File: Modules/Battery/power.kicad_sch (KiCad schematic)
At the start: 36 parts, among them IC3 TPS630701RNMR, J2 BATTERY, J3 POWER SWITCH, J4 TEMP SENSOR, Q1 T2N7002AK,LM, U203 AP2112K-3.3, U4 BQ24075RGT

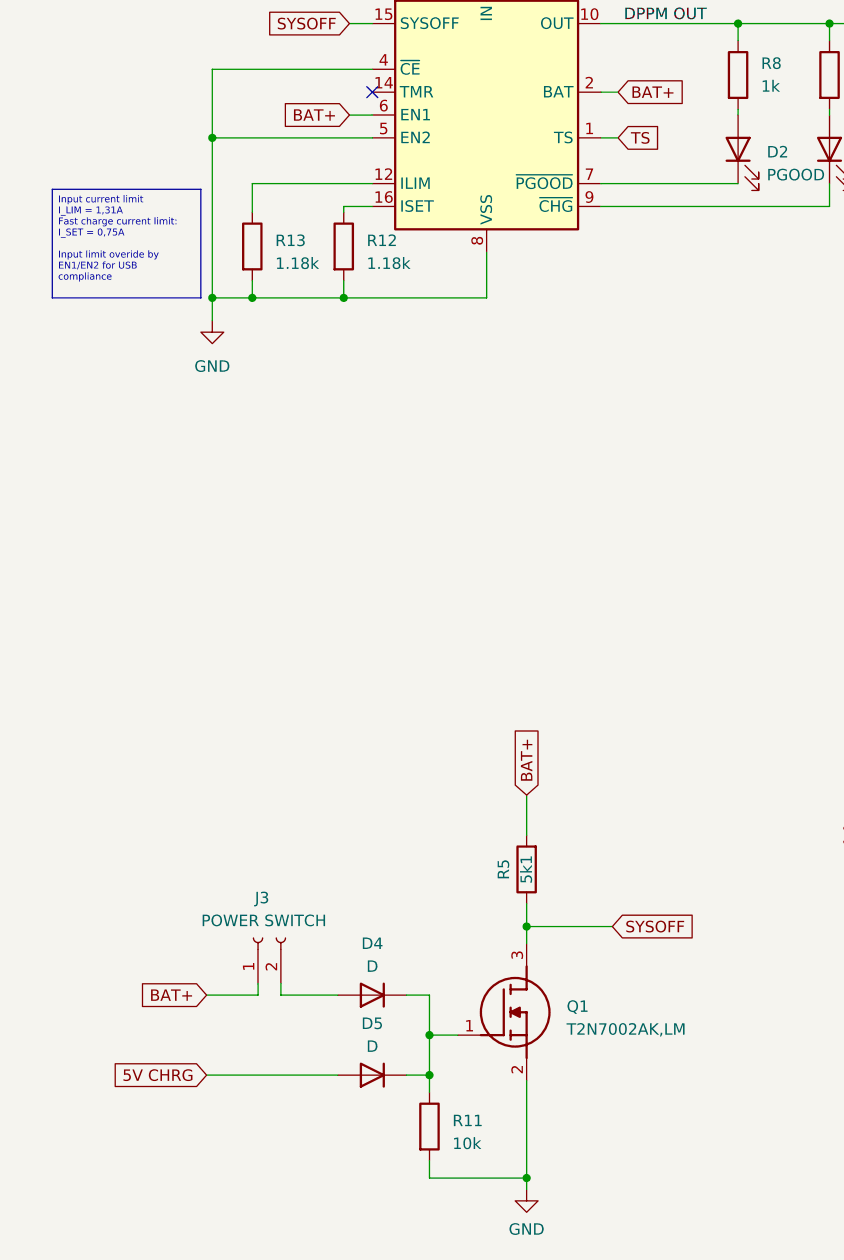
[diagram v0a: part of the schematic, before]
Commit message: update to I2C and MIDI Interface
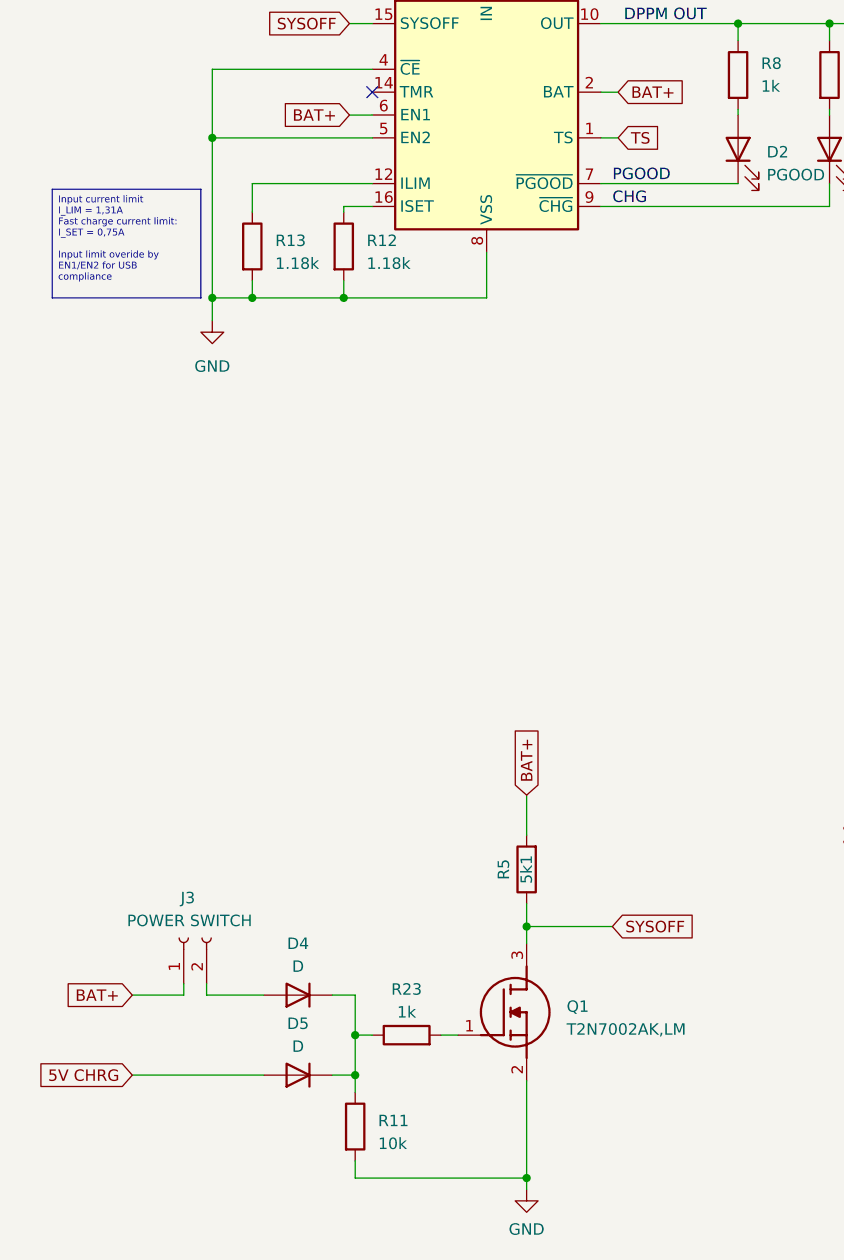
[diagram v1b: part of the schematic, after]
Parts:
- added R23: 1k, symbol Device:R
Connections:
- net CHG: now reaches D3.1 (K), U4.9 (~{CHG})
- net at D4.1 (K), D5.1 (K), R11.1: now also R23.1; no longer Q1.1 (G)
- net PGOOD: now reaches D2.1 (K), U4.7 (~{PGOOD})
- new net: Q1.1 (G), R23.2
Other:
- moved on the sheet: D4, D5, J3, R11

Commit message: first rev of Battery module
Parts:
- removed J3: POWER SWITCH, Connector_custom:PinHeader_1x02_P2.54mm_Horizontal_SMD, symbol Connector:Conn_01x02_Socket
- removed J4: TEMP SENSOR, symbol Connector:Conn_01x02_Socket
- added C4: 100n, Capacitor_SMD:C_0603_1608Metric, symbol Device:C
- added D6, D7: LED, LED_SMD:LED_0603_1608Metric, symbol Device:LED
- added J7: M20-8900505, Connector_Harwin:Harwin_M20-89005xx_1x05_P2.54mm_Horizontal, symbol Connector_Generic:Conn_01x05
- added R24, R25: 1k, Resistor_SMD:R_0603_1608Metric, symbol Device:R
- added SW3: POWER SWITCH, Switch footprints:SLW-864547-5A-RA-D, symbol Switch:SW_SPDT
- C3, C4, C8: footprint (none) -> Capacitor_SMD:C_0603_1608Metric
- D2: value PGOOD -> LED green; footprint LED_SMD:LED_0603_1608Metric_Pad1.05x0.95mm_HandSolder -> SamacSys:155124RS73200
- D3: value CHG -> LED red; footprint LED_SMD:LED_0603_1608Metric_Pad1.05x0.95mm_HandSolder -> SamacSys:155124RS73200
- D4, D5: value D -> RB21S30T5G; footprint Diode_SMD:D_0603_1608Metric -> Diode_SMD:D_SOD-523
- IC3: footprint TPS630701RNMR -> SamacSys:TPS630701RNMR
- L1: footprint (none) -> Inductor_SMD:L_0603_1608Metric
- L3: footprint (none) -> Inductor_custom:EATON_EXL1V0402_4.6mmx4.6mm
- Q1: footprint TBAT54CLM -> SamacSys:TBAT54CLM
- R11, R12, R13, R14, R15, R16, R23, R5: footprint (none) -> Resistor_SMD:R_0603_1608Metric
- R8, R9: value 1k -> 510; footprint Resistor_SMD:R_0603_1608Metric_Pad0.98x0.95mm_HandSolder -> Resistor_SMD:R_0603_1608Metric
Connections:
- net +3V3: now also D7.2 (A)
- net +5V: now also D6.2 (A), J7.1 (Pin_1)
- net 5V CHRG: now also J7.2 (Pin_2)
- net BAT+: now also SW3.2 (B)
- net DPPM OUT: now also C4.1
- net GND: now also C17.2, J2.2 (Pin_2), C4.2, J7.5 (Pin_5), R24.2, R25.2
- net at D4.2 (A): now also SW3.1 (A)
- new net: D7.1 (K), R25.1
- new net: D6.1 (K), R24.1
- new net SCL_5V: J7.4 (Pin_4)
- new net SDA_5V: J7.3 (Pin_3)
- no-connect marks 1 -> 2
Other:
- moved on the sheet: C16, C18, C19, C20, D3, R9
